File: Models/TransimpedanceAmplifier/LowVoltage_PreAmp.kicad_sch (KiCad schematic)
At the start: 3 parts, among them U7 LM7805, 5V, 5%, U9 LM7905, -5V, 5%

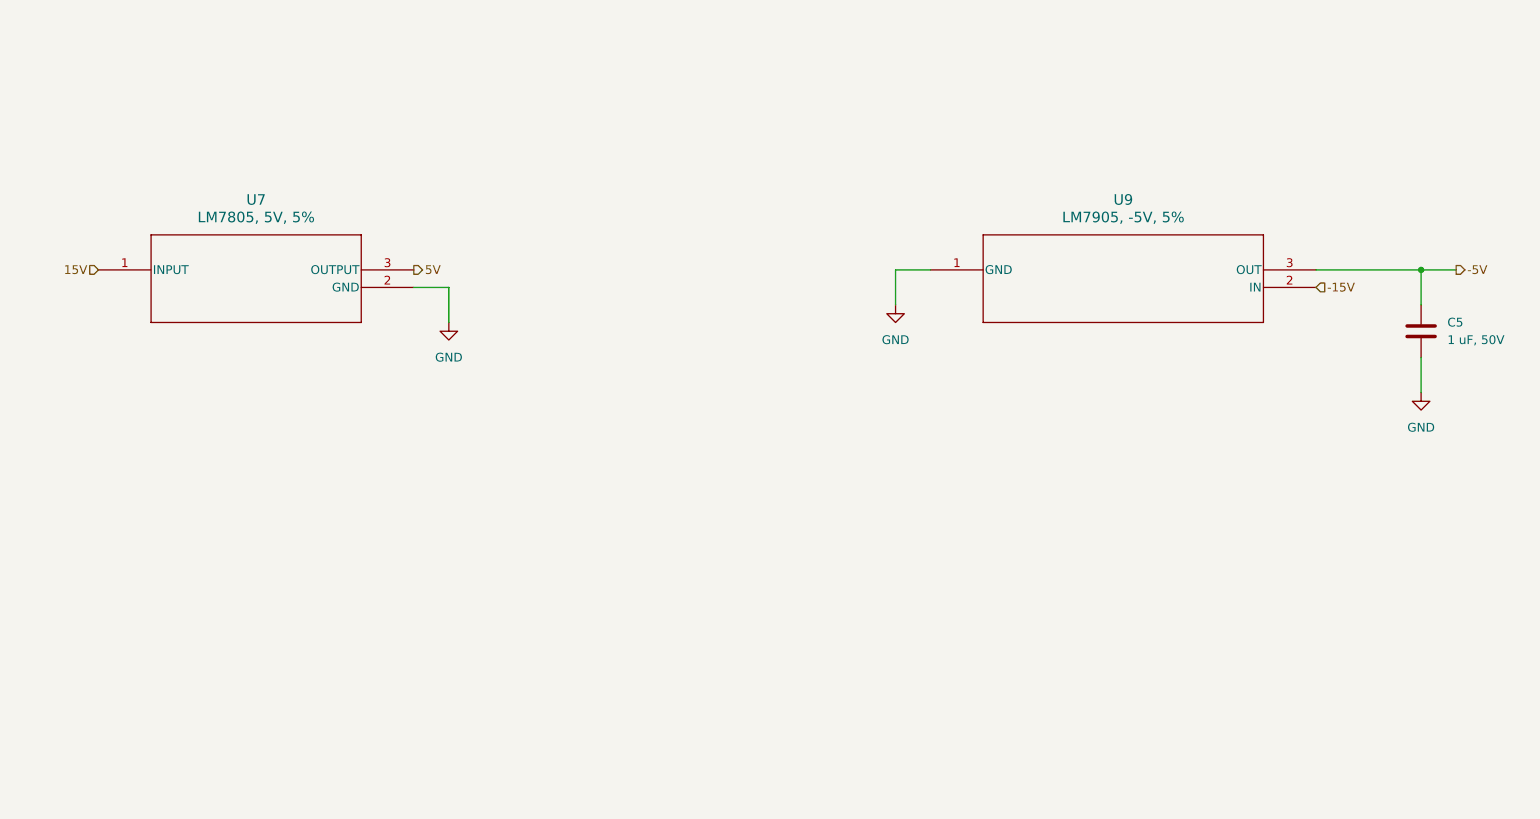
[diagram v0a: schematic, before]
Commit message: Finished the decoupling networks for the power subsystem
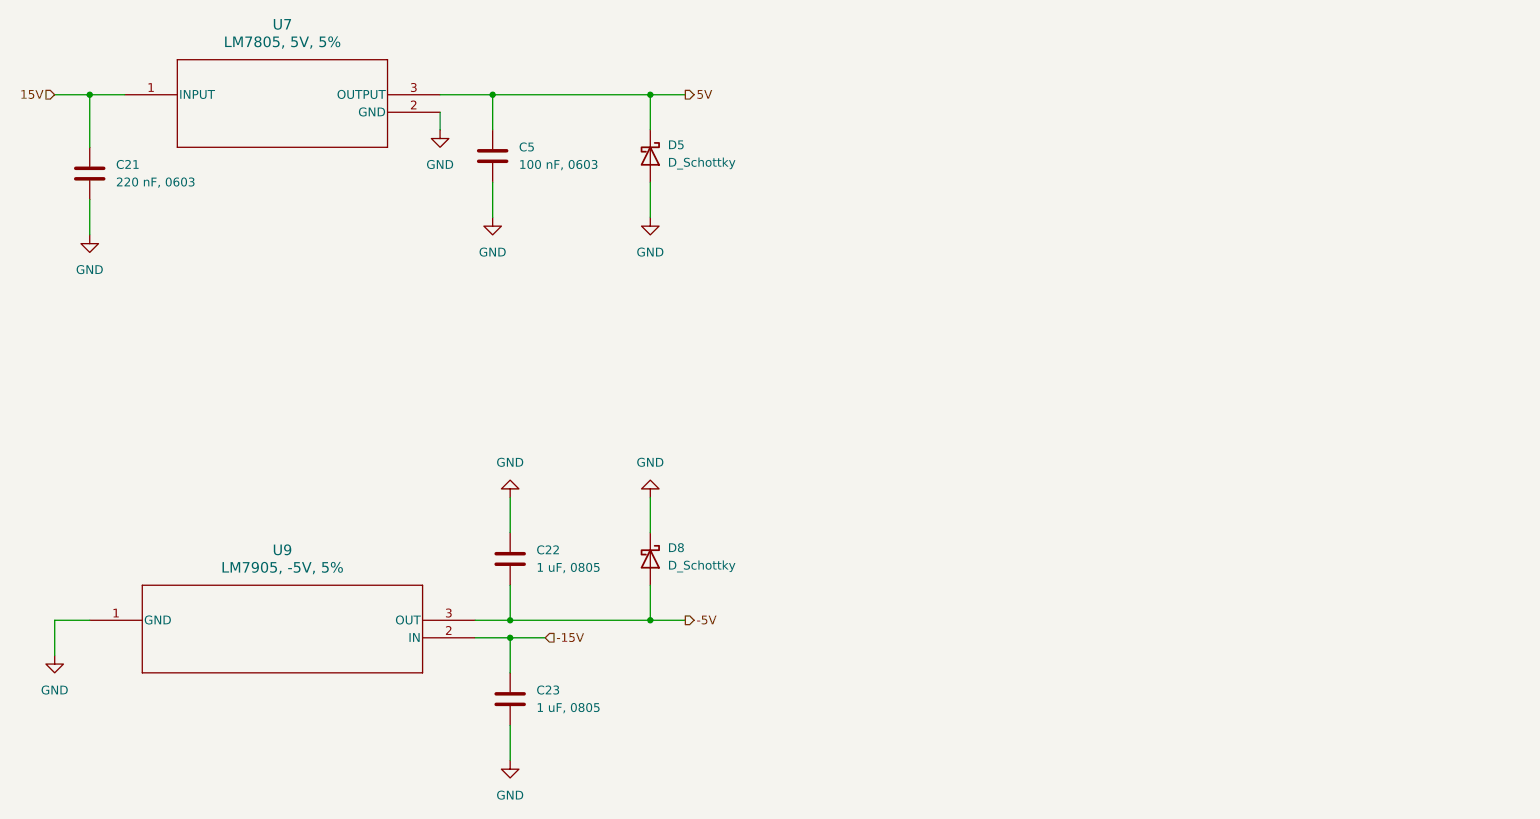
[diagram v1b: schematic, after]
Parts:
- added C21: 220 nF, 0603, symbol Device:C
- added C22, C23: 1 uF, 0805, symbol Device:C
- added D5, D8: D_Schottky, symbol Device:D_Schottky
- C5: value 1 uF, 50V -> 100 nF, 0603; Purchase Link https://www.digikey.com/en/products/detail/murata-electroni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 -> (none)
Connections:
- net -15V: now also C23.1
- net -5V: now also C22.2, D8.2 (A); no longer C5.1
- net 15V: now also C21.1
- net 5V: now also C5.1, D5.1 (K)
- net GND: now also C21.2, C22.1, C23.2, D5.2 (A), D8.1 (K)
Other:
- moved on the sheet: U7, U9

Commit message: Finished for today
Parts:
- C21, C22, C23, C5: Purchase Link (none) -> https://www.digikey.com/en/products/detail/murata-electroni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
- D5, D8: Purchase Link (none) -> https://www.digikey.com/en/products/detail/diodes-incorpora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
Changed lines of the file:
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@@
+			)
+		)
+		(property "Purchase Link" "https://www.digikey.com/en/products/detail/murata-electronics/GRM188R71H224KAC4D/5797498"
+			(at 53.34 67.31 0)
+			(effects
+				(font
+					(size 1.27 1.27)
+				)
+				(hide yes)
 			)
 		)
@@
 			)
 		)
+		(property "Purchase Link" "https://www.digikey.com/en/products/detail/murata-electronics/GRM188R72A104KA35D/702549"
+			(at 111.76 64.77 0)
+			(effects
+				(font
+					(size 1.27 1.27)
+				)
+				(hide yes)
+			)
+		)
 		(pin "1"
 		)
@@
 			)
 		)
+		(property "Purchase Link" "https://www.digikey.com/en/products/detail/murata-electronics/GRT21BR71H105KE01L/10702345"
+			(at 114.3 143.51 0)
+			(effects
+				(font
+					(size 1.27 1.27)
+				)
+				(hide yes)
+			)
+		)
 		(pin "1"
 		)
@@
 			)
 		)
+		(property "Purchase Link" "https://www.digikey.com/en/products/detail/diodes-incorporated/1N5819HW-7-F/814970"
+			(at 134.62 64.77 90)
+			(effects
+				(font
+					(size 1.27 1.27)
+				)
+				(hide yes)
+			)
+		)
 		(pin "1"
 		)
@@
 			)
 		)
+		(property "Purchase Link" "https://www.digikey.com/en/products/detail/murata-electronics/GRT21BR71H105KE01L/10702345"
+			(at 114.3 123.19 0)
+			(effects
+				(font
+					(size 1.27 1.27)
+				)
+				(hide yes)
+			)
+		)
 		(pin "1"
 		)
@@
 			(effects
 				(font
+					(size 1.27 1.27)
+				)
+				(hide yes)
+			)
+		)
+		(property "Purchase Link" "https://www.digikey.com/en/products/detail/diodes-incorporated/1N5819HW-7-F/814970"
+			(at 134.62 123.19 90)
+			(effects
+				(font

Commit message: Save progress
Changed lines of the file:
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@@
 	)
 	(symbol
+		(lib_name "D_Schottky_1")
 		(lib_id "Device:D_Schottky")
 		(at 134.62 64.77 270)

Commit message: Save progress
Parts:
- U7: footprint NDE3_TEX -> (none)
- U9: footprint T03B_TEX -> (none)
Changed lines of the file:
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@@
 			)
 		)
-		(property "Footprint" "T03B_TEX"
+		(property "Footprint" ""
 			(at 53.34 132.08 0)
 			(effects
@@
 			)
 		)
-		(property "Footprint" "NDE3_TEX"
+		(property "Footprint" ""
 			(at 58.42 55.88 0)
 			(effects

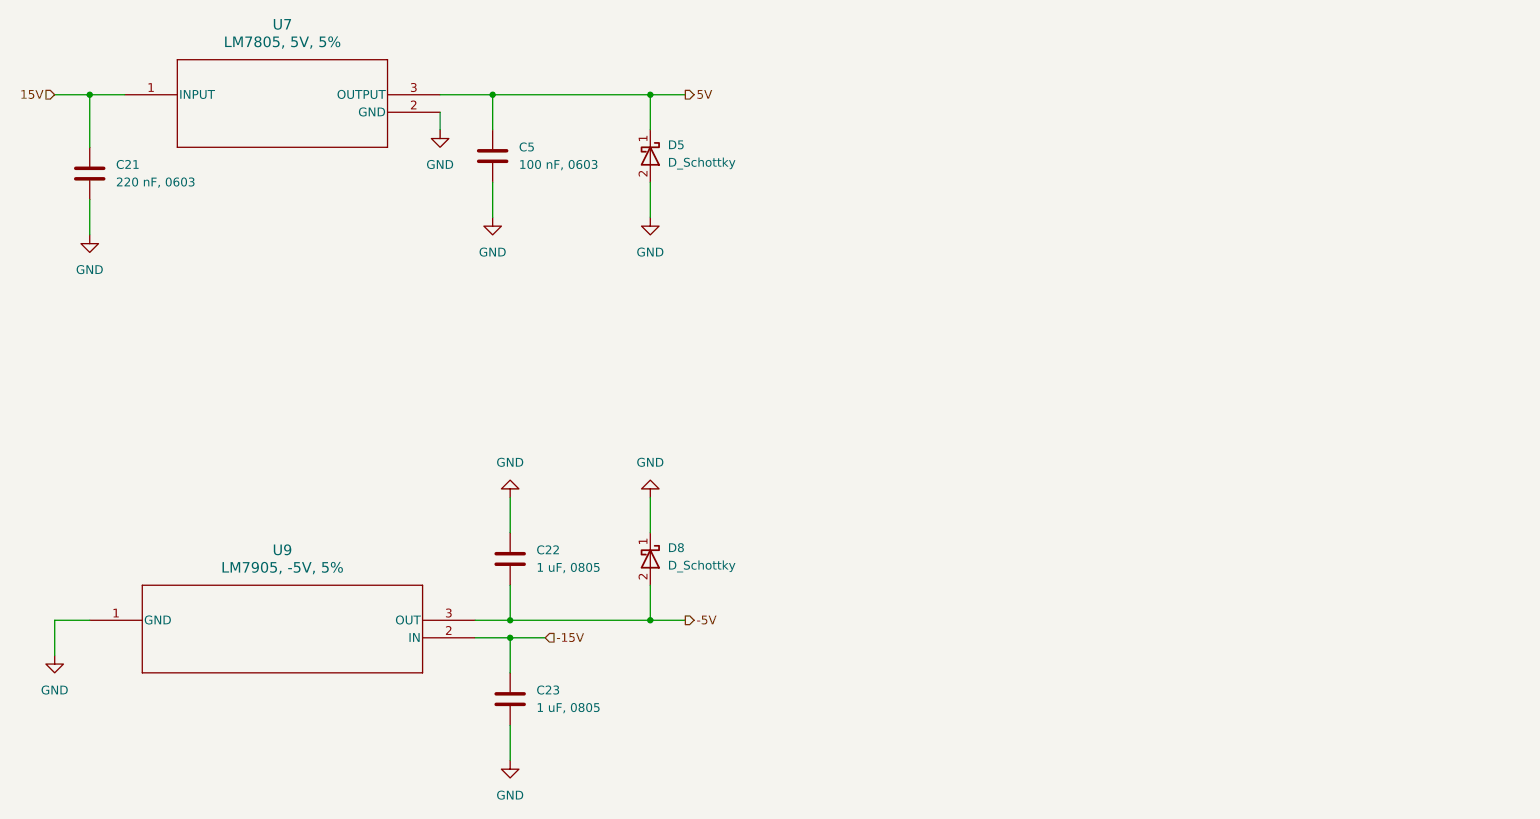
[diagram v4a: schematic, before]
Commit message: Overhauled all of the annotations
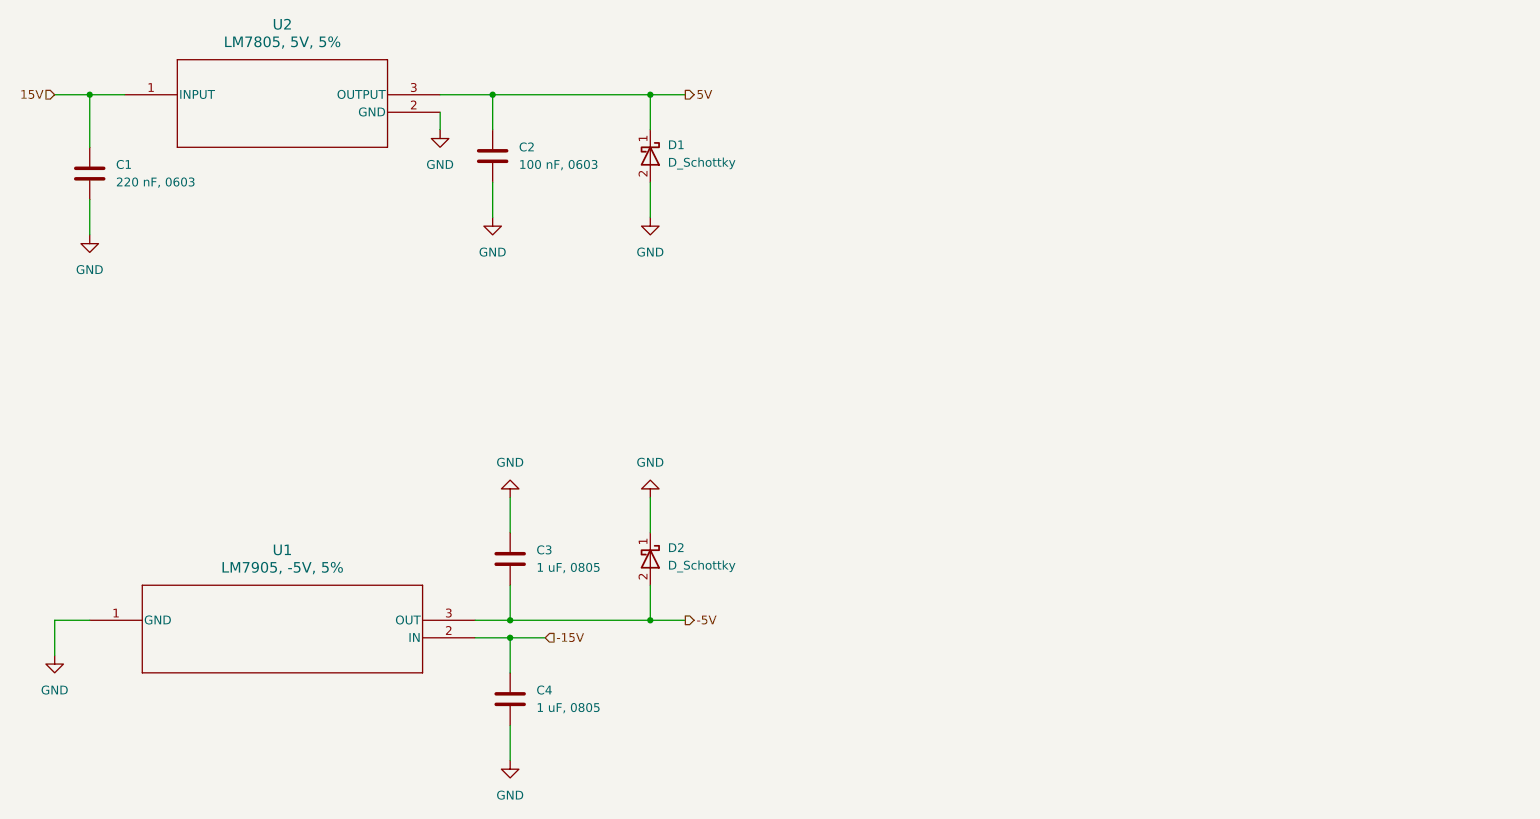
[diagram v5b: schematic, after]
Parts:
- renumbered C21 to C1, C5 to C2, C22 to C3, C23 to C4, D5 to D1, D8 to D2, U9 to U1, U7 to U2
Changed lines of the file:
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@@
 		(dnp no)
 		(fields_autoplaced yes)
-		(property "Reference" "#PWR028"
+		(property "Reference" "#PWR09"
 			(at 114.3 158.75 0)
 			(effects
@@
 			(project ""
 				(path "/ec9f2ae3-e40d-40eb-9760-2b611ee8efd1/d0ece2d4-5b22-4822-ad0c-e2361683ec3d/ddbdd109-856f-45b9-b116-121e4fcc3b3f"
-					(reference "#PWR028")
+					(reference "#PWR09")
 					(unit 1)
 				)
@@
 		(dnp no)
 		(fields_autoplaced yes)
-		(property "Reference" "#PWR011"
+		(property "Reference" "#PWR010"
 			(at 134.62 80.01 0)
 			(effects
@@
 			(project ""
 				(path "/ec9f2ae3-e40d-40eb-9760-2b611ee8efd1/d0ece2d4-5b22-4822-ad0c-e2361683ec3d/ddbdd109-856f-45b9-b116-121e4fcc3b3f"
-					(reference "#PWR011")
+					(reference "#PWR010")
 					(unit 1)
 				)
@@
 		(dnp no)
 		(fields_autoplaced yes)
-		(property "Reference" "C21"
+		(property "Reference" "C1"
 			(at 57.15 66.0399 0)
 			(effects
@@
 			(project ""
 				(path "/ec9f2ae3-e40d-40eb-9760-2b611ee8efd1/d0ece2d4-5b22-4822-ad0c-e2361683ec3d/ddbdd109-856f-45b9-b116-121e4fcc3b3f"
-					(reference "C21")
+					(reference "C1")
 					(unit 1)
 				)
@@
 		(dnp no)
 		(fields_autoplaced yes)
-		(property "Reference" "C5"
+		(property "Reference" "C2"
 			(at 115.57 63.4999 0)
 			(effects
@@
 			(project ""
 				(path "/ec9f2ae3-e40d-40eb-9760-2b611ee8efd1/d0ece2d4-5b22-4822-ad0c-e2361683ec3d/ddbdd109-856f-45b9-b116-121e4fcc3b3f"
-					(reference "C5")
+					(reference "C2")
 					(unit 1)
 				)
@@
 		(dnp no)
 		(fields_autoplaced yes)
-		(property "Reference" "#PWR010"
+		(property "Reference" "#PWR04"
 			(at 48.26 143.51 0)
 			(effects
@@
 			(project ""
 				(path "/ec9f2ae3-e40d-40eb-9760-2b611ee8efd1/d0ece2d4-5b22-4822-ad0c-e2361683ec3d/ddbdd109-856f-45b9-b116-121e4fcc3b3f"
-					(reference "#PWR010")
+					(reference "#PWR04")
 					(unit 1)
 				)
@@
 		(dnp no)
 		(fields_autoplaced yes)
-		(property "Reference" "C23"
+		(property "Reference" "C4"
 			(at 118.11 142.2399 0)
 			(effects
@@
 			(project "TransimpedanceAmplifier"
 				(path "/ec9f2ae3-e40d-40eb-9760-2b611ee8efd1/d0ece2d4-5b22-4822-ad0c-e2361683ec3d/ddbdd109-856f-45b9-b116-121e4fcc3b3f"
-					(reference "C23")
+					(reference "C4")
 					(unit 1)
 				)
@@
 		(dnp no)
 		(fields_autoplaced yes)
-		(property "Reference" "#PWR09"
+		(property "Reference" "#PWR06"
 			(at 104.14 67.31 0)
 			(effects
@@
 			(project ""
 				(path "/ec9f2ae3-e40d-40eb-9760-2b611ee8efd1/d0ece2d4-5b22-4822-ad0c-e2361683ec3d/ddbdd109-856f-45b9-b116-121e4fcc3b3f"
-					(reference "#PWR09")
+					(reference "#PWR06")
 					(unit 1)
 				)
@@
 		(dnp no)
 		(fields_autoplaced yes)
-		(property "Reference" "#PWR029"
+		(property "Reference" "#PWR08"
 			(at 114.3 107.95 0)
 			(effects
@@
 			(project ""
 				(path "/ec9f2ae3-e40d-40eb-9760-2b611ee8efd1/d0ece2d4-5b22-4822-ad0c-e2361683ec3d/ddbdd109-856f-45b9-b116-121e4fcc3b3f"
-					(reference "#PWR029")
+					(reference "#PWR08")
 					(unit 1)
 				)
@@
 		(dnp no)
 		(fields_autoplaced yes)
-		(property "Reference" "#PWR027"
+		(property "Reference" "#PWR05"
 			(at 53.34 82.55 0)
 			(effects
@@
 			(project ""
 				(path "/ec9f2ae3-e40d-40eb-9760-2b611ee8efd1/d0ece2d4-5b22-4822-ad0c-e2361683ec3d/ddbdd109-856f-45b9-b116-121e4fcc3b3f"
-					(reference "#PWR027")
+					(reference "#PWR05")
 					(unit 1)
 				)
@@
 		(dnp no)
 		(fields_autoplaced yes)
-		(property "Reference" "D5"
+		(property "Reference" "D1"
 			(at 137.16 63.1824 90)
 			(effects
@@
 			(project ""
 				(path "/ec9f2ae3-e40d-40eb-9760-2b611ee8efd1/d0ece2d4-5b22-4822-ad0c-e2361683ec3d/ddbdd109-856f-45b9-b116-121e4fcc3b3f"
-					(reference "D5")
+					(reference "D1")
 					(unit 1)
 				)
@@
 		(dnp no)
 		(fields_autoplaced yes)
-		(property "Reference" "C22"
+		(property "Reference" "C3"
 			(at 118.11 121.9199 0)
 			(effects
@@
 			(project ""
 				(path "/ec9f2ae3-e40d-40eb-9760-2b611ee8efd1/d0ece2d4-5b22-4822-ad0c-e2361683ec3d/ddbdd109-856f-45b9-b116-121e4fcc3b3f"
-					(reference "C22")
+					(reference "C3")
 					(unit 1)
 				)
@@
 		(dnp no)
 		(fields_autoplaced yes)
-		(property "Reference" "#PWR037"
+		(property "Reference" "#PWR011"
 			(at 134.62 107.95 0)
 			(effects
@@
 			(project ""
 				(path "/ec9f2ae3-e40d-40eb-9760-2b611ee8efd1/d0ece2d4-5b22-4822-ad0c-e2361683ec3d/ddbdd109-856f-45b9-b116-121e4fcc3b3f"
-					(reference "#PWR037")
+					(reference "#PWR011")
 					(unit 1)
 				)
@@
 		(dnp no)
 		(fields_autoplaced yes)
-		(property "Reference" "#PWR036"
+		(property "Reference" "#PWR07"
 			(at 111.76 80.01 0)
 			(effects
@@
 			(project "TransimpedanceAmplifier"
 				(path "/ec9f2ae3-e40d-40eb-9760-2b611ee8efd1/d0ece2d4-5b22-4822-ad0c-e2361683ec3d/ddbdd109-856f-45b9-b116-121e4fcc3b3f"
-					(reference "#PWR036")
+					(reference "#PWR07")
 					(unit 1)
 				)
@@
 		(dnp no)
 		(fields_autoplaced yes)
-		(property "Reference" "U9"
+		(property "Reference" "U1"
 			(at 81.28 121.92 0)
 			(effects
@@
 			(project ""
 				(path "/ec9f2ae3-e40d-40eb-9760-2b611ee8efd1/d0ece2d4-5b22-4822-ad0c-e2361683ec3d/ddbdd109-856f-45b9-b116-121e4fcc3b3f"
-					(reference "U9")
+					(reference "U1")
 					(unit 1)
 				)
@@
 		(dnp no)
 		(fields_autoplaced yes)
-		(property "Reference" "D8"
+		(property "Reference" "D2"
 			(at 137.16 121.6024 90)
 			(effects
@@
 			(project "TransimpedanceAmplifier"
 				(path "/ec9f2ae3-e40d-40eb-9760-2b611ee8efd1/d0ece2d4-5b22-4822-ad0c-e2361683ec3d/ddbdd109-856f-45b9-b116-121e4fcc3b3f"
-					(reference "D8")
+					(reference "D2")
 					(unit 1)
 				)
@@
 		(dnp no)
 		(fields_autoplaced yes)
-		(property "Reference" "U7"
+		(property "Reference" "U2"
 			(at 81.28 45.72 0)
 			(effects
@@
 			(project ""
 				(path "/ec9f2ae3-e40d-40eb-9760-2b611ee8efd1/d0ece2d4-5b22-4822-ad0c-e2361683ec3d/ddbdd109-856f-45b9-b116-121e4fcc3b3f"
-					(reference "U7")
-					(unit 1)
-				)
+					(reference "U2")
+					(unit 1)
+				)
